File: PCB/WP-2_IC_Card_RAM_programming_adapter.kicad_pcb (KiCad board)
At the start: 2 copper layers, 17.8 x 49.5 mm, 2 parts, among them J1 Conn_01x38_Male, J2 Conn_02x16_Counter_Clockwise

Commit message: readme
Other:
- board text added: "In programmer set device = 628128"
- board text removed: "FOR RAM CARD NOT ROM"
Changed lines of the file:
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@@
     (add_net /A15)
     (add_net /A16)
-    (add_net /A17)
     (add_net /A2)
     (add_net /A3)
@@
     (add_net /A8)
     (add_net /A9)
-    (add_net /BCHK)
     (add_net /D0)
     (add_net /D1)
@@
     (add_net /VDD)
     (add_net /~CE1)
-    (add_net /~DET)
     (add_net /~OE)
     (add_net GND)
-    (add_net "Net-(J1-Pad15)")
-    (add_net "Net-(J1-Pad16)")
-    (add_net "Net-(J1-Pad3)")
-    (add_net "Net-(J1-Pad36)")
-    (add_net "Net-(J2-Pad1)")
   )
   (module 0_LOCAL:Pin_Header_Straight_1x38_Pitch1.27mm (layer F.Cu)
@@
     )
   )
-  (gr_text "FOR RAM CARD NOT ROM" (at 136.436 99.695 -90) (layer F.SilkS)
-    (effects (font (size 1.6 1.6) (thickness 0.2)))
+  (gr_text "In programmer set device = 628128" (at 135.436 99.695 -90) (layer F.SilkS)
+    (effects (font (size 1.2 1.2) (thickness 0.2)))
   )
   (gr_line (start 132.066 78.74) (end 133.336 78.74) (layer Edge.Cuts) (width 0.1))
@@
   (gr_line (start 133.336 120.015) (end 130.886 120.015) (layer B.SilkS) (width 0.15))
   (gr_line (start 133.336 79.375) (end 133.336 120.015) (layer B.SilkS) (width 0.15))
+  (segment (start 147.256 85.725) (end 147.306 85.725) (width 0.2032) (layer B.Cu) (net 0))
+  (segment (start 147.226 85.695) (end 147.256 85.725) (width 0.2032) (layer B.Cu) (net 0))
   (segment (start 138.924 76.2) (end 139.686 76.2) (width 0.3048) (layer B.Cu) (net 1))
   (segment (start 138.543 76.581) (end 138.924 76.2) (width 0.3048) (layer B.Cu) (net 1))
@@
   (segment (start 132.066 83.185) (end 137.908 89.027) (width 0.18) (layer B.Cu) (net 11))
   (segment (start 147.306 83.185) (end 147.196 83.185) (width 0.18) (layer F.Cu) (net 12))
+  (segment (start 140.686 89.805) (end 147.306 83.185) (width 0.18) (layer B.Cu) (net 12))
+  (segment (start 140.686 98.195) (end 140.686 89.805) (width 0.18) (layer B.Cu) (net 12))
+  (segment (start 139.821 99.06) (end 140.686 98.195) (width 0.18) (layer B.Cu) (net 12))
+  (segment (start 139.686 99.06) (end 139.821 99.06) (width 0.18) (layer B.Cu) (net 12))
   (segment (start 138.186 98.83) (end 139.686 100.33) (width 0.18) (layer B.Cu) (net 13))
   (segment (start 138.186 93.695) (end 138.186 98.83) (width 0.18) (layer B.Cu) (net 13))
@@
   (segment (start 143.786 84.11) (end 143.786 105.845) (width 0.18) (layer F.Cu) (net 30))
   (segment (start 139.686 80.01) (end 143.786 84.11) (width 0.18) (layer F.Cu) (net 30))
-  (segment (start 147.256 85.725) (end 147.306 85.725) (width 0.2032) (layer B.Cu) (net 0))
-  (segment (start 147.226 85.695) (end 147.256 85.725) (width 0.2032) (layer B.Cu) (net 0))
-  (segment (start 140.686 89.805) (end 147.306 83.185) (width 0.18) (layer B.Cu) (net 12))
-  (segment (start 140.686 98.195) (end 140.686 89.805) (width 0.18) (layer B.Cu) (net 12))
-  (segment (start 139.821 99.06) (end 140.686 98.195) (width 0.18) (layer B.Cu) (net 12))
-  (segment (start 139.686 99.06) (end 139.821 99.06) (width 0.18) (layer B.Cu) (net 12))
 )

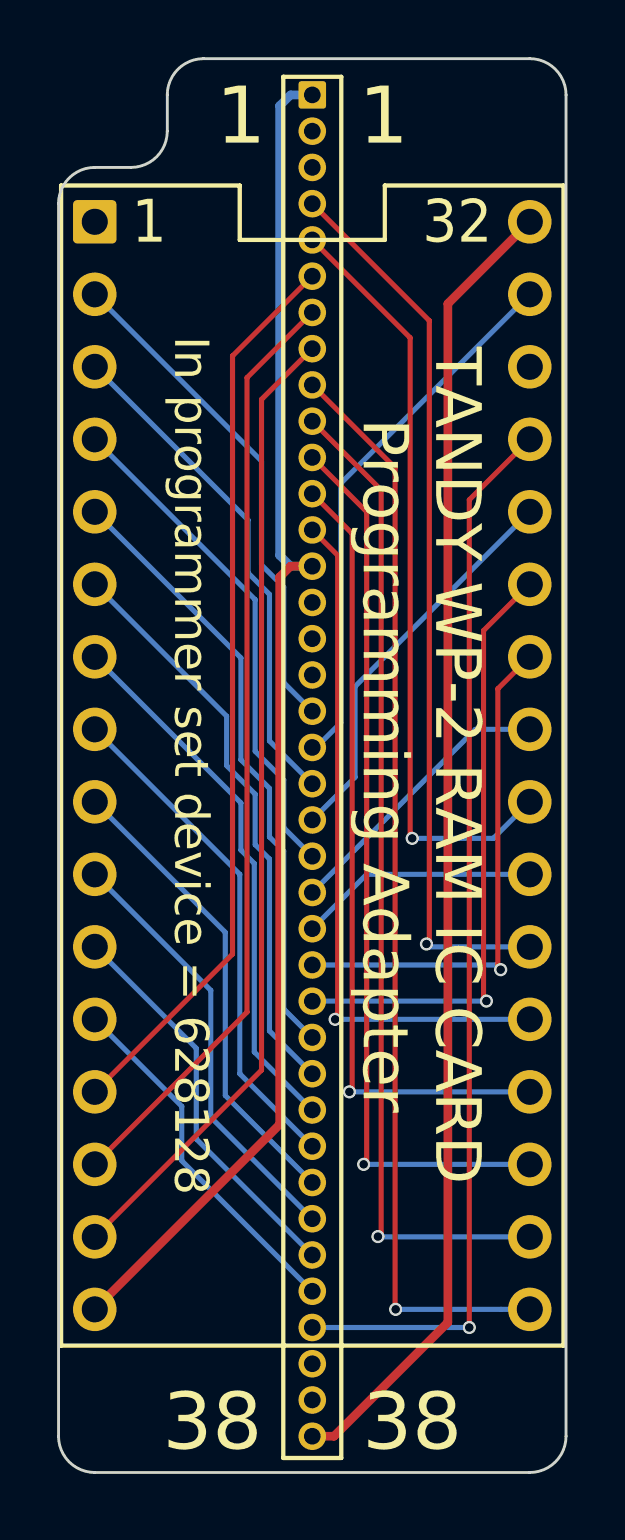
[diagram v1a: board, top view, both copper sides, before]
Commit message: fix wiring error on write-enable switch on ram card
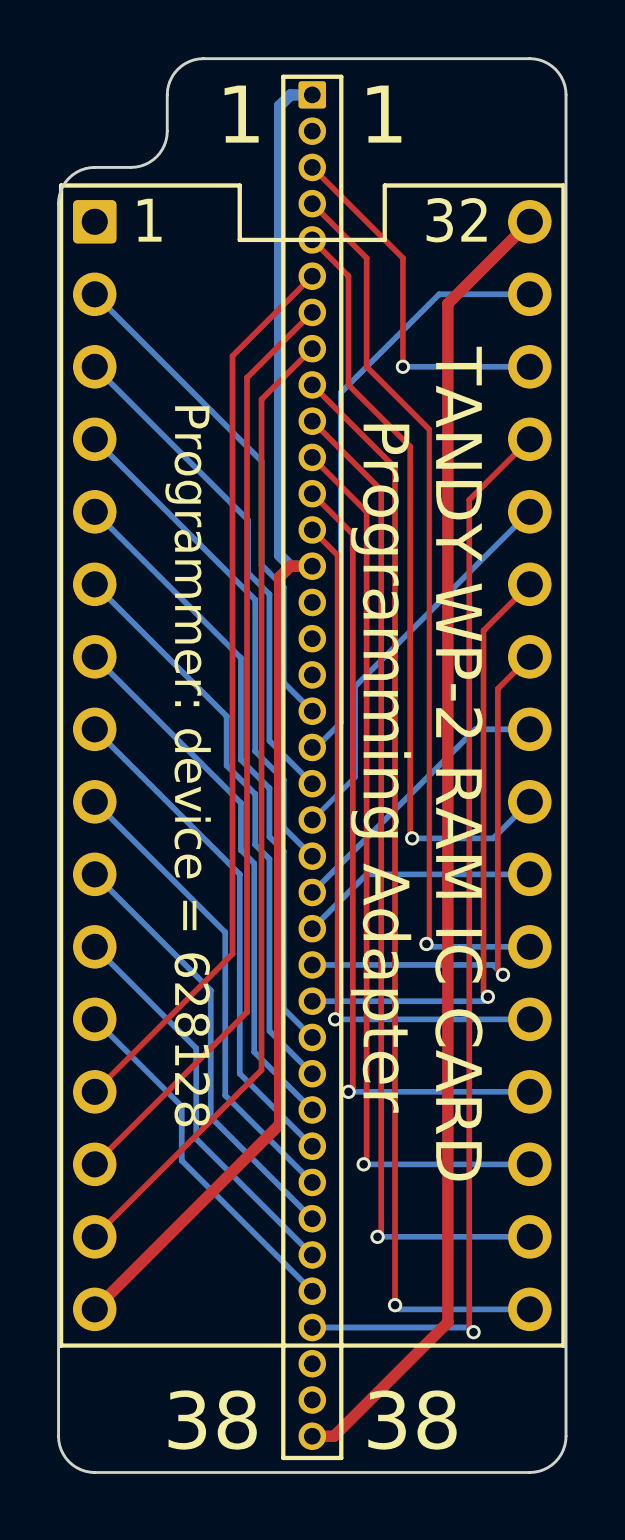
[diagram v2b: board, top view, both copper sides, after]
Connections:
- net /VDD renamed VDD
- J1 pad 3: (no net) -> /CE2
- J2 pad 30: (no net) -> /CE2
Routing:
- net /CE2: track 0.00 -> 12.7 mm, vias 0 -> 1
- net /A15: track 19.2 -> 21.0 mm
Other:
- net class Default: clearance 0.16 -> 0.2; trace_width 0.18 -> 0.2; via_dia 0.46 -> 0.5
- rule trace_clearance: 0.16 -> 0.2
- rule trace_min: 0.16 -> 0.2
- rule via_min_drill: 0.25 -> 0.3
- rule via_min_size: 0.4 -> 0.5
- board text added: "Programmer: device = 628128"
- board text added: "WP-2_IC_Card_RAM_programming_adapter v002"
- board text removed: "In programmer set device = 628128"
- board text removed: "WP-2_IC_Card_RAM_programming_adapter v001"
